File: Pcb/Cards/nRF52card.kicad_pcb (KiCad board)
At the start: 2 copper layers, 45.7 x 36.8 mm, 8 parts, among them J1 CA6_02X06, J2 NFC_ANT, J3 PROG_01X06, U1 SN74AHC1G08, U2 BL652-SA-01, X1 HOLE

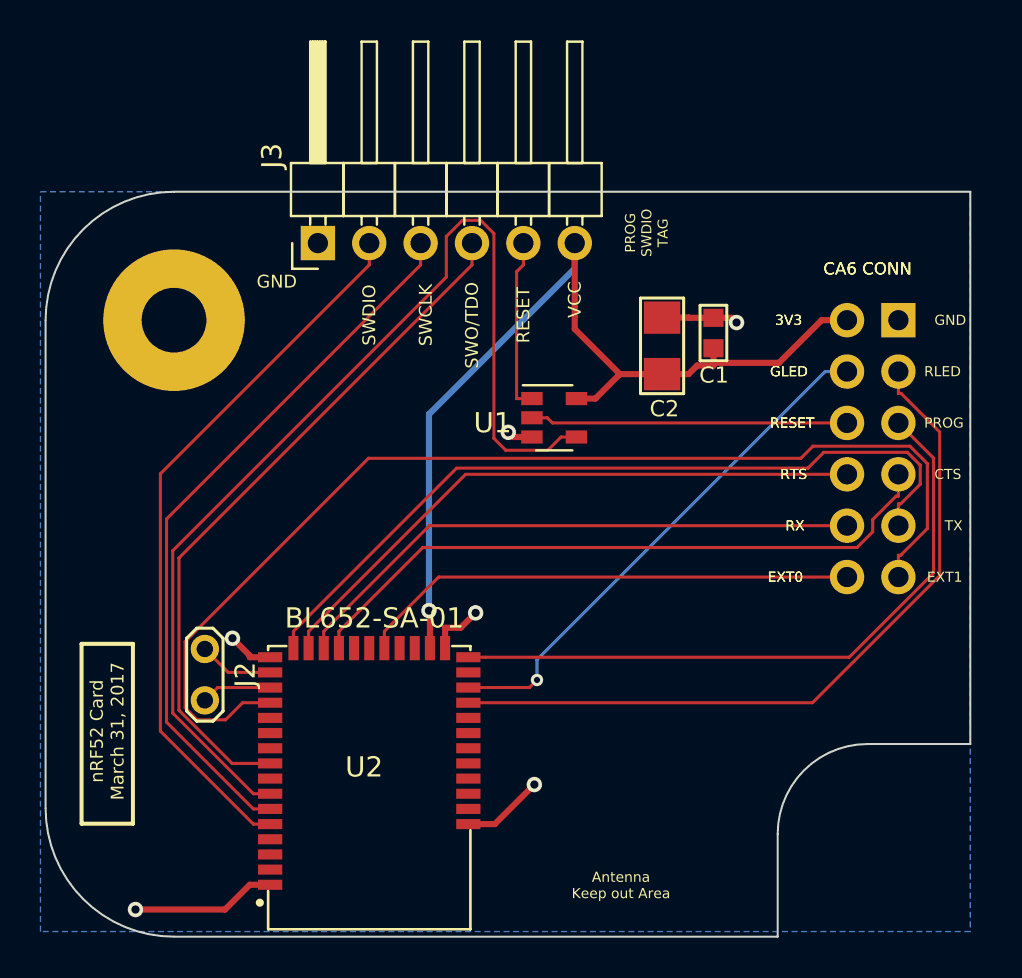
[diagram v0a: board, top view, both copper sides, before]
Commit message: Updated all text on both ESP8266card and nRF52card to minimum of .635x.635x.1524 (6 mils).  Verified that all pins chosen on nRF52 can be used as general IO if we're not using smartBasic (which we probably won't be using), so I didn't change any of them.
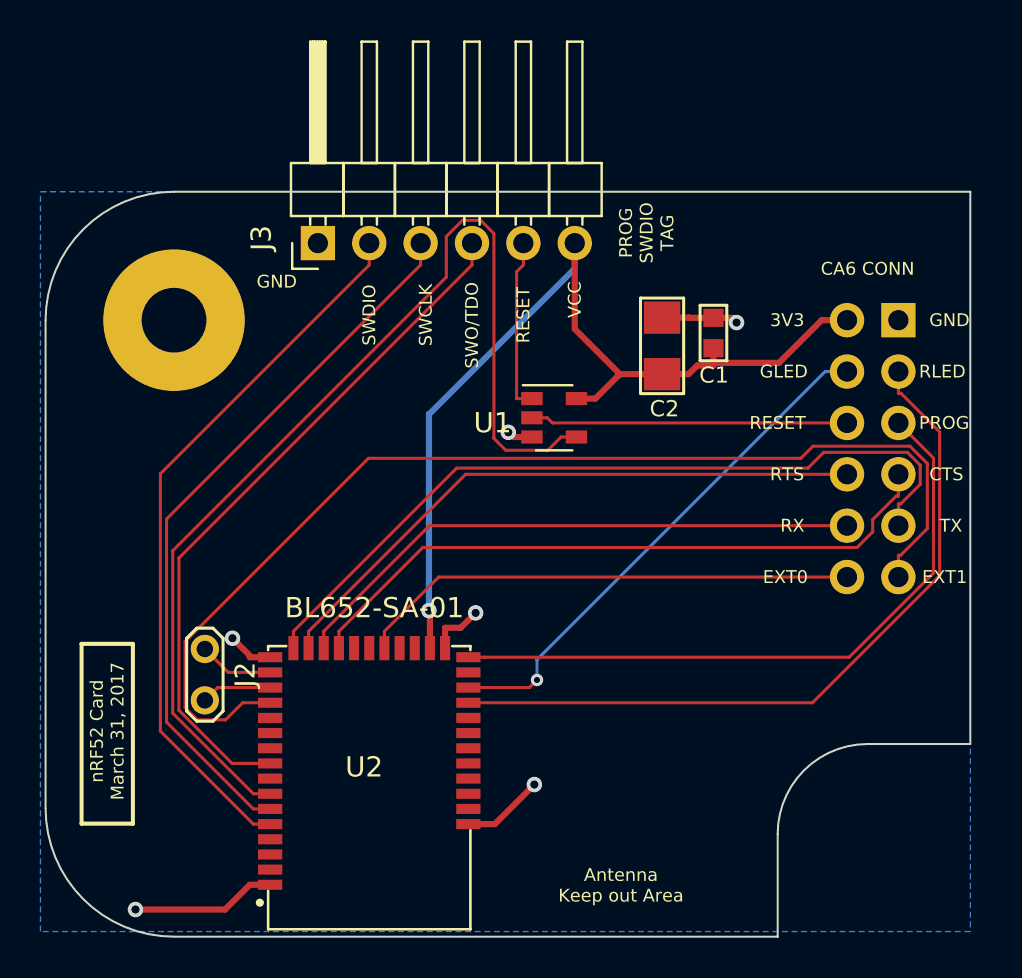
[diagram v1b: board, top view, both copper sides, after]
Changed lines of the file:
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@@
     (area 152.146 90.920999 199.490001 139.78)
     (thickness 1.6)
-    (drawings 48)
+    (drawings 41)
     (tracks 140)
     (zones 0)
@@
     (uvia_min_size 0.6096)
     (uvia_min_drill 0.3556)
-    (pcb_text_width 0.3)
-    (pcb_text_size 1.5 1.5)
+    (pcb_text_width 0.1524)
+    (pcb_text_size 0.635 0.635)
     (mod_edge_width 0.15)
     (mod_text_size 1 1)
@@
     (attr smd)
     (fp_text reference U2 (at 0.254 1.016 180) (layer F.SilkS)
-      (effects (font (size 1 1) (thickness 0.05)))
-    )
-    (fp_text value BL652-SA-01 (at -0.254 8.382 180) (layer F.SilkS)
-      (effects (font (size 1 1) (thickness 0.05)))
+      (effects (font (size 1 1) (thickness 0.15)))
+    )
+    (fp_text value BL652-SA-01 (at -0.254 8.89 180) (layer F.SilkS)
+      (effects (font (size 1 1) (thickness 0.15)))
     )
     (fp_line (start 5 -7) (end -5 -7) (layer F.SilkS) (width 0.127))
@@
       (effects (font (size 1 1) (thickness 0.15)))
     )
-    (fp_text value SN74AHC1G08 (at 0 2.9) (layer F.Fab)
+    (fp_text value SN74AHC1G08 (at 0 2.9) (layer F.Fab) hide
       (effects (font (size 1 1) (thickness 0.15)))
     )
@@
     (descr "Through hole angled pin header, 1x06, 2.54mm pitch, 6mm pin length, single row")
     (tags "Through hole angled pin header THT 1x06 2.54mm single row")
-    (fp_text reference J3 (at 4.315 -2.27 90) (layer F.SilkS)
+    (fp_text reference J3 (at 0.254 -2.794 90) (layer F.SilkS)
       (effects (font (size 1 1) (thickness 0.15)))
     )
-    (fp_text value PROG_01X06 (at 4.315 14.97 90) (layer F.Fab)
+    (fp_text value PROG_01X06 (at 4.315 14.97 90) (layer F.Fab) hide
       (effects (font (size 1 1) (thickness 0.15)))
     )
@@
     (fp_line (start 10.4 14.5) (end 10.4 -1.8) (layer F.CrtYd) (width 0.05))
     (fp_line (start 10.4 -1.8) (end -1.8 -1.8) (layer F.CrtYd) (width 0.05))
-    (fp_text user %R (at 4.315 -2.27 90) (layer F.Fab)
+    (fp_text user %R (at 0.254 -2.794 90) (layer F.Fab)
       (effects (font (size 1 1) (thickness 0.15)))
     )
@@
     )
     (fp_text value NFC_ANT (at 1.27 2 270) (layer F.Fab)
-      (effects (font (size 1 1) (thickness 0.15)))
+      (effects (font (size 0.635 0.635) (thickness 0.1524)))
     )
     (fp_line (start -0.65 1.15) (end 3.15 1.15) (layer F.CrtYd) (width 0.05))
@@
     )
   )
-  (gr_text 3V3 (at 188.468 105.41) (layer F.SilkS)
-    (effects (font (size 0.5 0.5) (thickness 0.1)) (justify left))
-  )
-  (gr_text GLED (at 188.214 107.95) (layer F.SilkS)
-    (effects (font (size 0.5 0.5) (thickness 0.1)) (justify left))
-  )
-  (gr_text RESET (at 188.214 110.49) (layer F.SilkS)
-    (effects (font (size 0.5 0.5) (thickness 0.1)) (justify left))
-  )
-  (gr_text RTS (at 188.722 113.03) (layer F.SilkS)
-    (effects (font (size 0.5 0.5) (thickness 0.1)) (justify left))
-  )
-  (gr_text RX (at 188.976 115.57) (layer F.SilkS)
-    (effects (font (size 0.5 0.5) (thickness 0.1)) (justify left))
-  )
   (gr_text "CA6 CONN" (at 193.04 102.87) (layer F.SilkS)
-    (effects (font (size 0.6 0.6) (thickness 0.1)))
+    (effects (font (size 0.635 0.635) (thickness 0.1524)))
+  )
+  (gr_text "PROG\nSWDIO\nTAG" (at 182.118 101.092 90) (layer F.SilkS)
+    (effects (font (size 0.635 0.635) (thickness 0.1524)))
   )
   (gr_text EXT0 (at 188.976 118.11) (layer F.SilkS)
-    (effects (font (size 0.5 0.5) (thickness 0.1)))
-  )
-  (gr_text "PROG\nSWDIO\nTAG" (at 182.118 101.092 90) (layer F.SilkS)
-    (effects (font (size 0.5 0.5) (thickness 0.1)))
-  )
-  (gr_text EXT0 (at 188.976 118.11) (layer F.SilkS)
-    (effects (font (size 0.5 0.5) (thickness 0.1)))
+    (effects (font (size 0.635 0.635) (thickness 0.1524)))
   )
   (gr_text EXT1 (at 196.85 118.11) (layer F.SilkS)
-    (effects (font (size 0.5 0.5) (thickness 0.1)))
-  )
-  (gr_text "CA6 CONN" (at 193.04 102.87) (layer F.SilkS)
-    (effects (font (size 0.6 0.6) (thickness 0.1)))
+    (effects (font (size 0.635 0.635) (thickness 0.1524)))
   )
   (gr_text VCC (at 178.562 104.394 90) (layer F.SilkS)
-    (effects (font (size 0.635 0.635) (thickness 0.15)))
+    (effects (font (size 0.635 0.635) (thickness 0.1524)))
   )
   (gr_text RESET (at 176.022 105.156 90) (layer F.SilkS)
-    (effects (font (size 0.635 0.635) (thickness 0.15)))
+    (effects (font (size 0.635 0.635) (thickness 0.1524)))
   )
   (gr_text SWDIO (at 168.402 105.156 90) (layer F.SilkS)
-    (effects (font (size 0.635 0.635) (thickness 0.15)))
+    (effects (font (size 0.635 0.635) (thickness 0.1524)))
   )
   (gr_text "Antenna\nKeep out Area" (at 180.848 133.35) (layer F.SilkS)
-    (effects (font (size 0.5 0.5) (thickness 0.1)))
+    (effects (font (size 0.635 0.635) (thickness 0.1524)))
   )
   (gr_arc (start 158.75 129.54) (end 158.75 135.89) (angle 90) (layer Edge.Cuts) (width 0.099822))
@@
     (effects (font (size 0.635 0.635) (thickness 0.1524)))
   )
-  (gr_text RX (at 188.976 115.57) (layer F.SilkS)
-    (effects (font (size 0.5 0.5) (thickness 0.1)) (justify left))
-  )
-  (gr_text TX (at 196.85 115.57) (layer F.SilkS)
-    (effects (font (size 0.5 0.5) (thickness 0.1)) (justify left))
-  )
-  (gr_text RTS (at 188.722 113.03) (layer F.SilkS)
-    (effects (font (size 0.5 0.5) (thickness 0.1)) (justify left))
-  )
-  (gr_text CTS (at 196.342 113.03) (layer F.SilkS)
-    (effects (font (size 0.5 0.5) (thickness 0.1)) (justify left))
-  )
-  (gr_text RESET (at 188.214 110.49) (layer F.SilkS)
-    (effects (font (size 0.5 0.5) (thickness 0.1)) (justify left))
-  )
-  (gr_text PROG (at 195.834 110.49) (layer F.SilkS)
-    (effects (font (size 0.5 0.5) (thickness 0.1)) (justify left))
-  )
-  (gr_text GLED (at 188.214 107.95) (layer F.SilkS)
-    (effects (font (size 0.5 0.5) (thickness 0.1)) (justify left))
-  )
-  (gr_text RLED (at 195.834 107.95) (layer F.SilkS)
-    (effects (font (size 0.5 0.5) (thickness 0.1)) (justify left))
-  )
-  (gr_text 3V3 (at 188.468 105.41) (layer F.SilkS)
-    (effects (font (size 0.5 0.5) (thickness 0.1)) (justify left))
-  )
-  (gr_text GND (at 196.342 105.41) (layer F.SilkS)
-    (effects (font (size 0.5 0.5) (thickness 0.1)) (justify left))
+  (gr_text RX (at 188.722 115.57) (layer F.SilkS)
+    (effects (font (size 0.635 0.635) (thickness 0.1524)) (justify left))
+  )
+  (gr_text TX (at 196.596 115.57) (layer F.SilkS)
+    (effects (font (size 0.635 0.635) (thickness 0.1524)) (justify left))
+  )
+  (gr_text RTS (at 188.214 113.03) (layer F.SilkS)
+    (effects (font (size 0.635 0.635) (thickness 0.1524)) (justify left))
+  )
+  (gr_text CTS (at 196.088 113.03) (layer F.SilkS)
+    (effects (font (size 0.635 0.635) (thickness 0.1524)) (justify left))
+  )
+  (gr_text RESET (at 187.198 110.49) (layer F.SilkS)
+    (effects (font (size 0.635 0.635) (thickness 0.1524)) (justify left))
+  )
+  (gr_text PROG (at 195.58 110.49) (layer F.SilkS)
+    (effects (font (size 0.635 0.635) (thickness 0.1524)) (justify left))
+  )
+  (gr_text GLED (at 187.706 107.95) (layer F.SilkS)
+    (effects (font (size 0.635 0.635) (thickness 0.1524)) (justify left))
+  )
+  (gr_text RLED (at 195.58 107.95) (layer F.SilkS)
+    (effects (font (size 0.635 0.635) (thickness 0.1524)) (justify left))
+  )
+  (gr_text 3V3 (at 188.214 105.41) (layer F.SilkS)
+    (effects (font (size 0.635 0.635) (thickness 0.1524)) (justify left))
+  )
+  (gr_text GND (at 196.088 105.41) (layer F.SilkS)
+    (effects (font (size 0.635 0.635) (thickness 0.1524)) (justify left))
   )
   (gr_text SWCLK (at 171.196 105.156 90) (layer F.SilkS)
-    (effects (font (size 0.635 0.635) (thickness 0.15)))
+    (effects (font (size 0.635 0.635) (thickness 0.1524)))
   )
   (gr_text SWO/TDO (at 173.482 105.664 90) (layer F.SilkS)
@@
   (gr_line (start 194.31 137.16) (end 163.83 137.16) (angle 90) (layer Eco1.User) (width 0.2))
   (gr_line (start 199.39 132.08) (end 199.39 101.6) (angle 90) (layer Eco1.User) (width 0.2))
-  (gr_text "notch for screw\non CA6 brd" (at 193.294 130.81) (layer Dwgs.User)
-    (effects (font (size 0.508 0.508) (thickness 0.127)))
+  (gr_text "notch for screw\non CA6 brd" (at 193.294 130.81) (layer Eco1.User)
+    (effects (font (size 0.635 0.635) (thickness 0.1524)))
   )
   (gr_line (start 152.4 105.41) (end 152.4 129.54) (angle 90) (layer Edge.Cuts) (width 0.1))

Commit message: corrected labelling of EXT pins on both nRF52card and ESP8266card and rerouted some traces on nRF52card for better ground pour.
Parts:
- moved C1 18.1 mm to (173.5, 119.6), turned to 180 degrees
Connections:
- J1 pad 11: /CC_EXT1 -> /CC_EXT0
- J1 pad 12: /CC_EXT0 -> /CC_EXT1
- U2 pad 13: /CC_EXT1 -> /CC_EXT0
- U2 pad 23: /CC_EXT0 -> /CC_EXT1
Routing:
- net /CC_EXT0: track 24.8 -> 55.8 mm
- net /CC_EXT1: track 55.4 -> 27.8 mm
- net 3V3: track 46.2 -> 42.1 mm, vias 1 -> 2
- net /CC_CTS: track 32.7 -> 35.4 mm
- net /CC_RX: track 28.9 -> 30.7 mm
- net /CC_G_LED: track 25.8 -> 27.0 mm, vias 1 -> 3
- net GND: track 21.4 -> 22.1 mm

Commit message: Change clearance from 10 mil to 9 mil for thicker traces.  Fixes some DRC errors
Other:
- net class Thicker: clearance 0.254 -> 0.2286
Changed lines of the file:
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@@
-(kicad_pcb (version 4) (host pcbnew 4.0.6)
+(kicad_pcb (version 4) (host pcbnew 4.0.5)
   (general
     (links 30)
@@
   )
   (net_class Thicker ""
-    (clearance 0.254)
+    (clearance 0.2286)
     (trace_width 0.3048)
     (via_dia 0.762)
